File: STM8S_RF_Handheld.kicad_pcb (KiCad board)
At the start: 2 copper layers, 61 parts, among them IC1 STM8S003F3P, P1 CONN_01X02, P2 CONN_01X04, P3 CONN_01X04, P4 CONN_01X03, Q1 2SC1815, SW1 SW_SPDT, SW2 SW_PUSH, SW3 SW_PUSH, SW4 SW_PUSH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

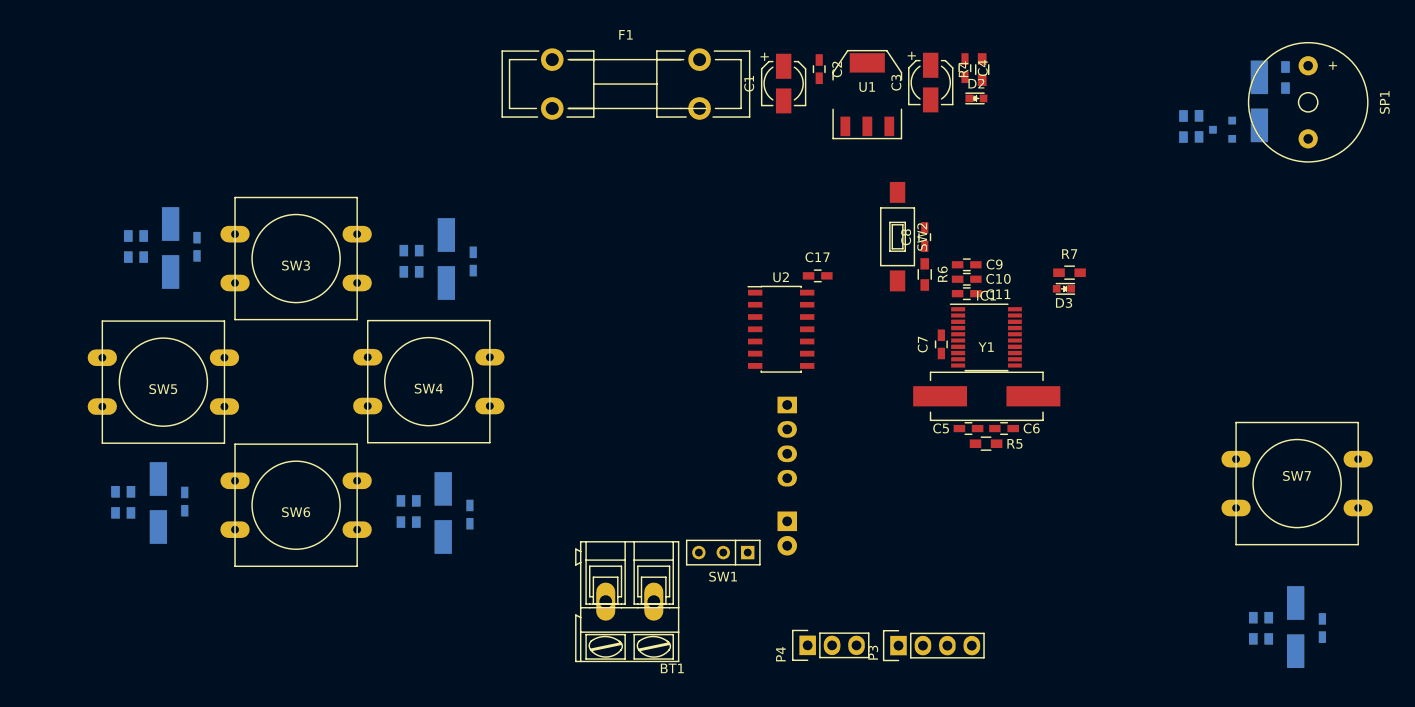
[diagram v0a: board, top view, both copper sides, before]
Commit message: Change PCB size.
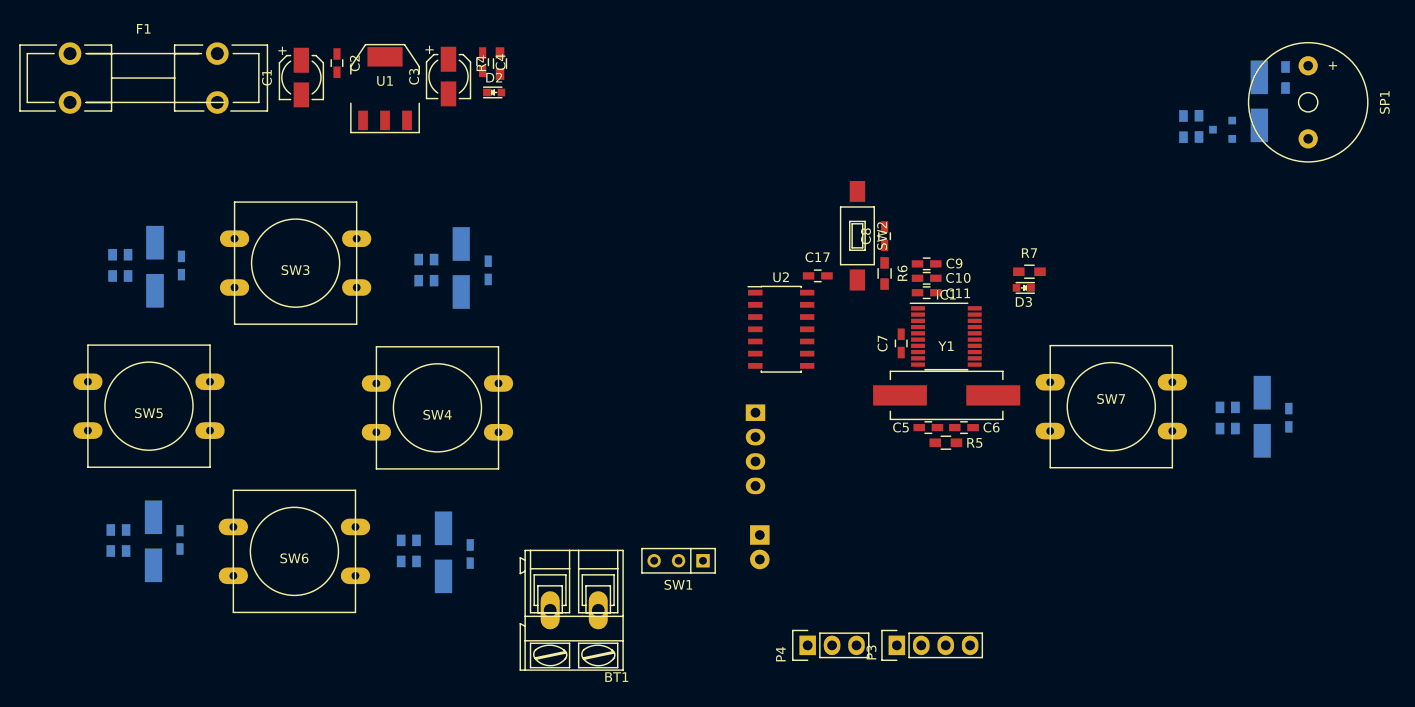
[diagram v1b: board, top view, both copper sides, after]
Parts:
- moved C1 50.2 mm to (81.8, 70.2)
- moved C3 50.2 mm to (97.2, 70.1)
- moved D2 50.2 mm to (101.9, 71.8)
- moved R4 50.2 mm to (102.5, 68.8)
- moved C2 50.2 mm to (85.5, 68.7)
- moved C4 50.2 mm to (100.7, 68.6)
- moved F1 50.2 mm to (65.5, 70.3)
- moved U1 50.2 mm to (90.5, 71.4)
- moved C16 22.1 mm to (184.6, 105.6)
- moved D8 22.1 mm to (181.8, 105.5)
- moved R12 22.1 mm to (177.4, 105.6)
- moved R17 22.1 mm to (179.0, 105.6)
- moved SW7 20.9 mm to (166.1, 104.5)
- moved BT1 5.84 mm to (112.7, 125.6)
- moved SW6 4.80 mm to (81.1, 119.5)
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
